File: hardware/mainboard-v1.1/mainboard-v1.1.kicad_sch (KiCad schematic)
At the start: 21 parts, among them J1 Conn_01x01, J2 Conn_01x01, J3 Conn_01x03, J4 Conn_01x03, J5 Conn_01x05, SW1 SW_SPDT, SW2 SW_SPST, SW3 SW_SPST, SW4 SW_SPST, SW5 SW_SPST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

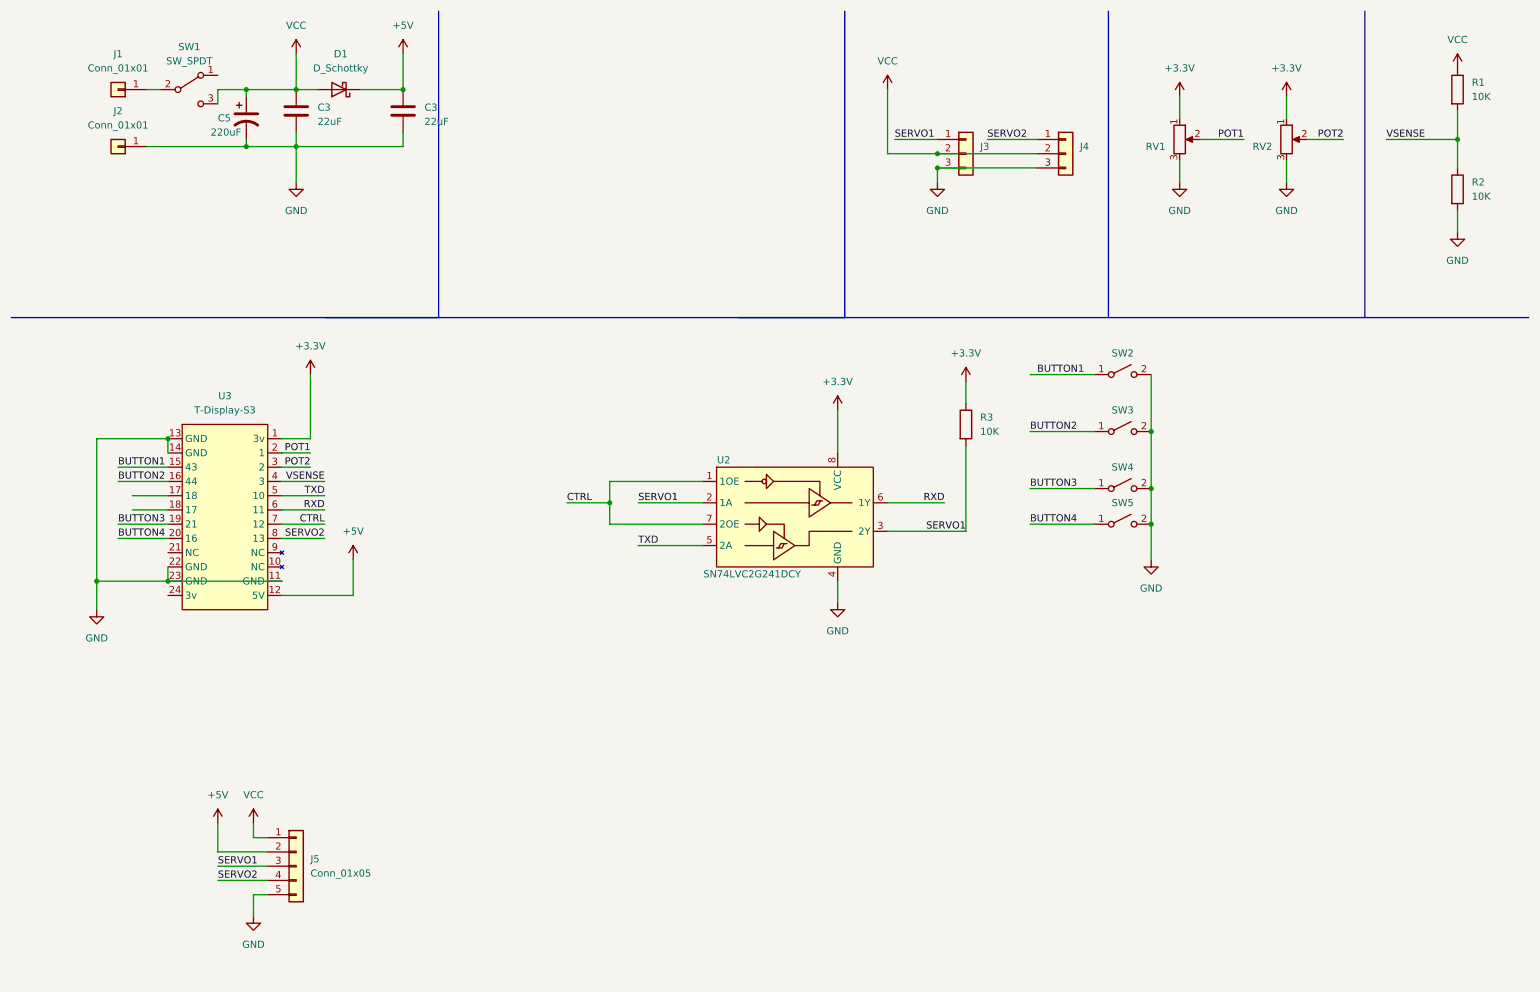
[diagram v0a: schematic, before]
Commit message: updating firmware for v 1.1
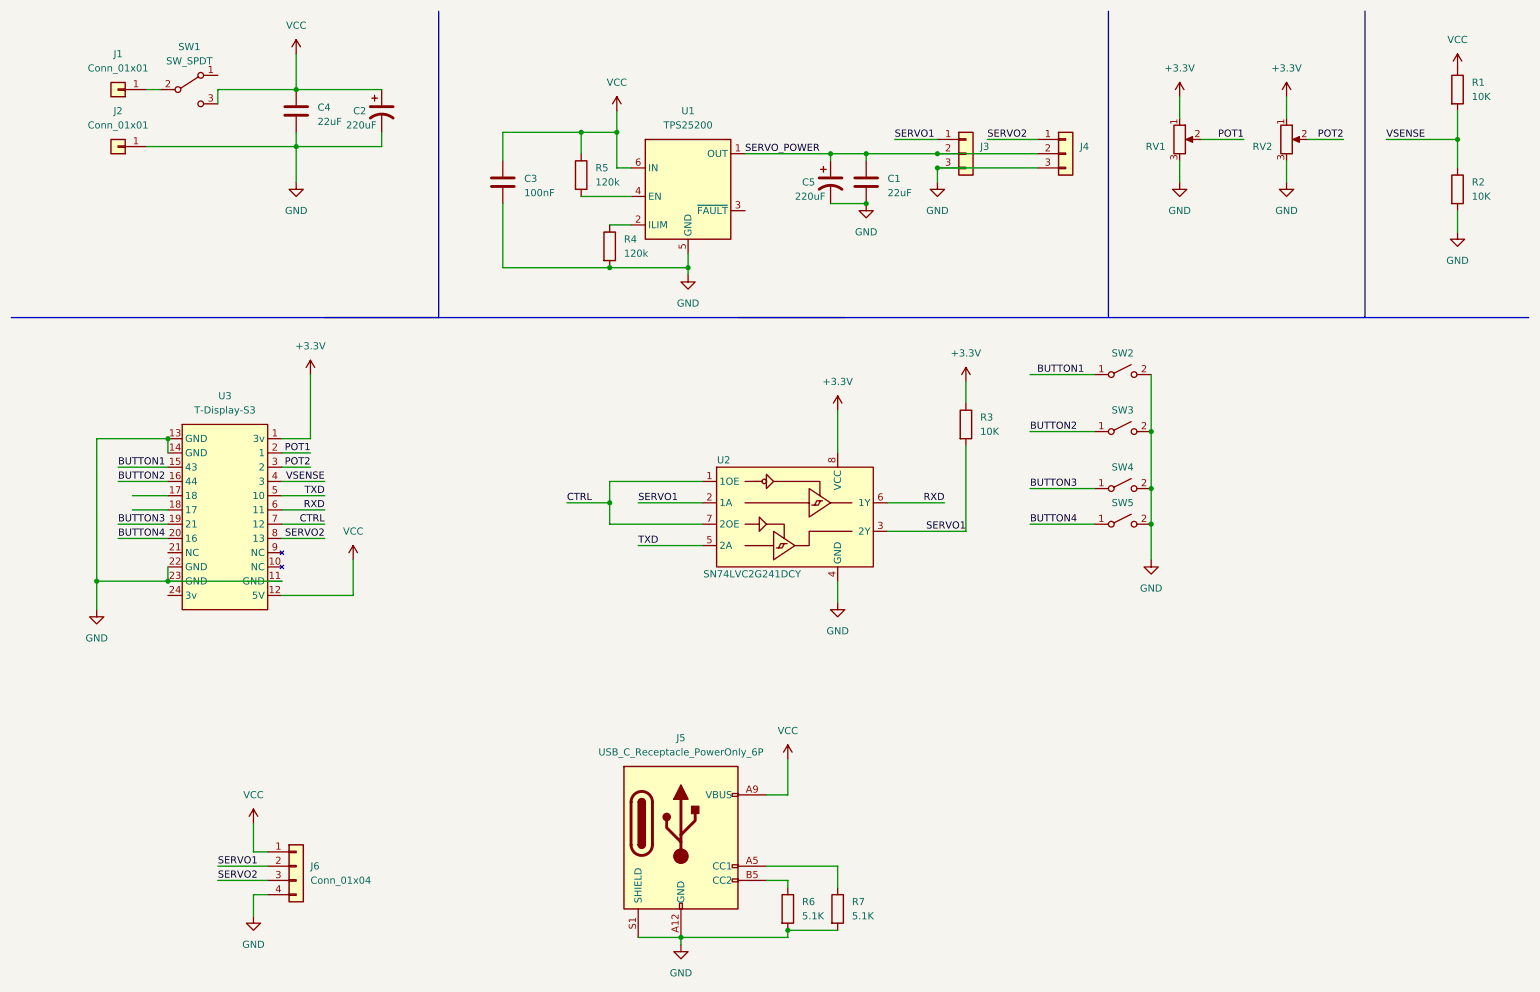
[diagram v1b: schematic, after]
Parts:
- removed D1: D_Schottky, Diode_SMD:D_SOD-323, symbol Device:D_Schottky
- removed J5: Conn_01x05, Connector_PinSocket_2.54mm:PinSocket_1x05_P2.54mm_Vertical, symbol Connector_Generic:Conn_01x05
- added C1: 22uF, Capacitor_SMD:C_0805_2012Metric, symbol Device:C
- added C2: 220uF, Capacitor_SMD:CP_Elec_6.3x7.7, symbol Device:C_Polarized_US
- added J5: USB_C_Receptacle_PowerOnly_6P, shurik-personal:USB_C_Receptacle_Korean_Hroparts-31-M-17, symbol Connector:USB_C_Receptacle_PowerOnly_6P
- added J6: Conn_01x04, shurik-personal:connector-4p-generic-nosilk, symbol Connector_Generic:Conn_01x04
- added R4, R5: 120k, Resistor_SMD:R_0603_1608Metric, symbol Device:R
- added R6, R7: 5.1K, Resistor_SMD:R_0603_1608Metric, symbol Device:R
- added U1: TPS25200, Package_SON:WSON-6-1EP_2x2mm_P0.65mm_EP1x1.6mm, symbol shurik-personal:TPS25200
- C3: value 22uF -> 100nF; footprint Capacitor_SMD:C_0805_2012Metric -> Capacitor_SMD:C_0603_1608Metric; LCSC C45783 -> C14663
- C5: FT Rotation Offset (none) -> 180; LCSC C131158 -> C96175
- J3, J4: FT Rotation Offset (none) -> 90; LCSC C49257 -> (none); LCSC PN (none) -> C2937625
- renumbered C3 to C4
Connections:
- net +5V is gone; now on net VCC: C4.1, U3.12 (5V)
- net GND: now also C1.2, C2.2, J5.A12 (GND), J5.B12 (GND), J5.S1 (SHIELD), J6.4 (Pin_4), R4.2, R6.2, R7.2, U1.5 (GND), U1.7 (GND)
- net SERVO1: now also J6.2 (Pin_2)
- net SERVO2: now also J6.3 (Pin_3)
- net VCC: now also C2.1, J5.A9 (VBUS), J5.B9 (VBUS), J6.1 (Pin_1), R5.1, U1.6 (IN); no longer C5.1, J3.2 (Pin_2), J4.2 (Pin_2)
- new net: J5.A5 (CC1), R7.1
- new net: J5.B5 (CC2), R6.1
- new net: R4.1, U1.2 (ILIM)
- new net: R5.2, U1.4 (EN)
- new net SERVO_POWER: C1.1, C5.1, J3.2 (Pin_2), J4.2 (Pin_2), U1.1 (OUT)
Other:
- moved on the sheet: C3, C4, C5
